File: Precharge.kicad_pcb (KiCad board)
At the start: 2 copper layers, 58 x 38 mm, 10 parts, among them J1 MicroFit+, J2 JST-XA, K1 DAR71205, Q1 BSS205N, U1 NCP1117

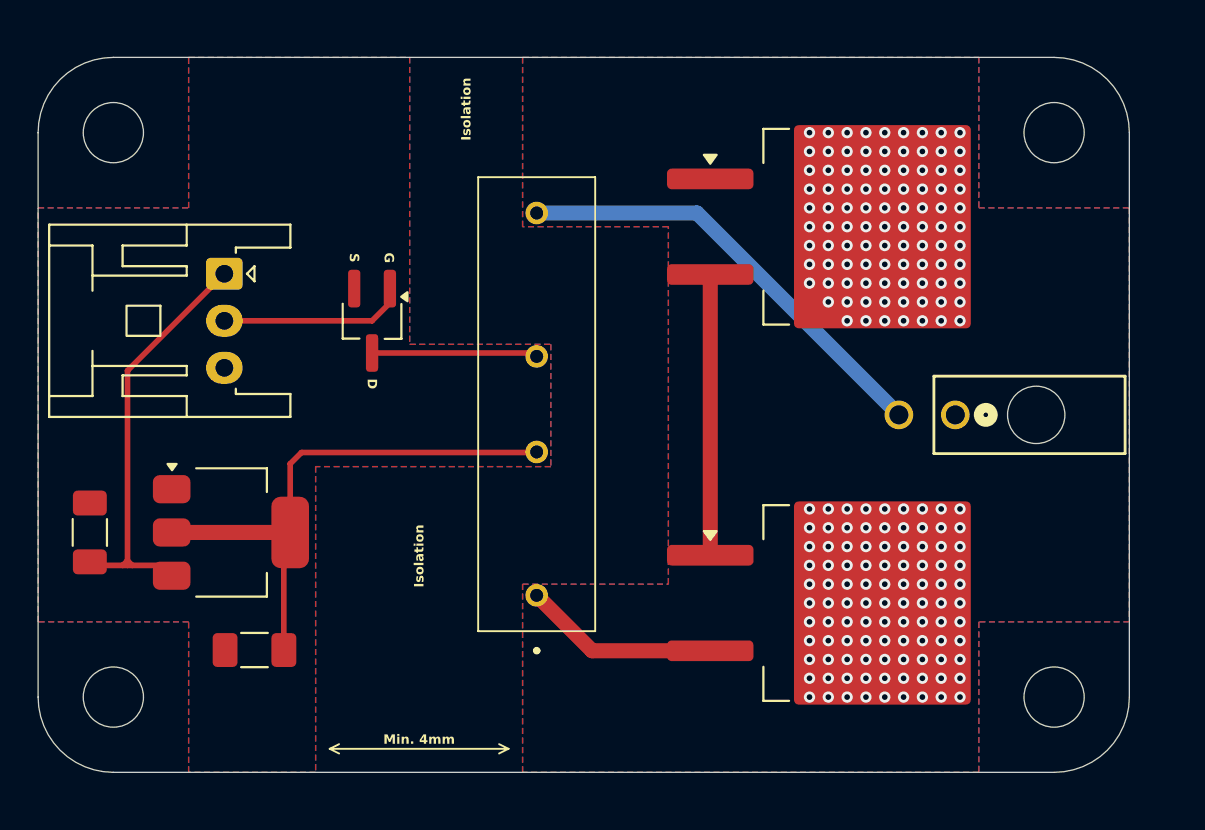
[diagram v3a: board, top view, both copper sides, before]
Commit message: TSAL compatibility, shortened precharge, simpler LV
Back to 4 resistors, so short precharge time, and powering relay from BMS GPIO. Cut SCS and regulation. added TSAL circuitry to allow for relay state measurement with single contact.
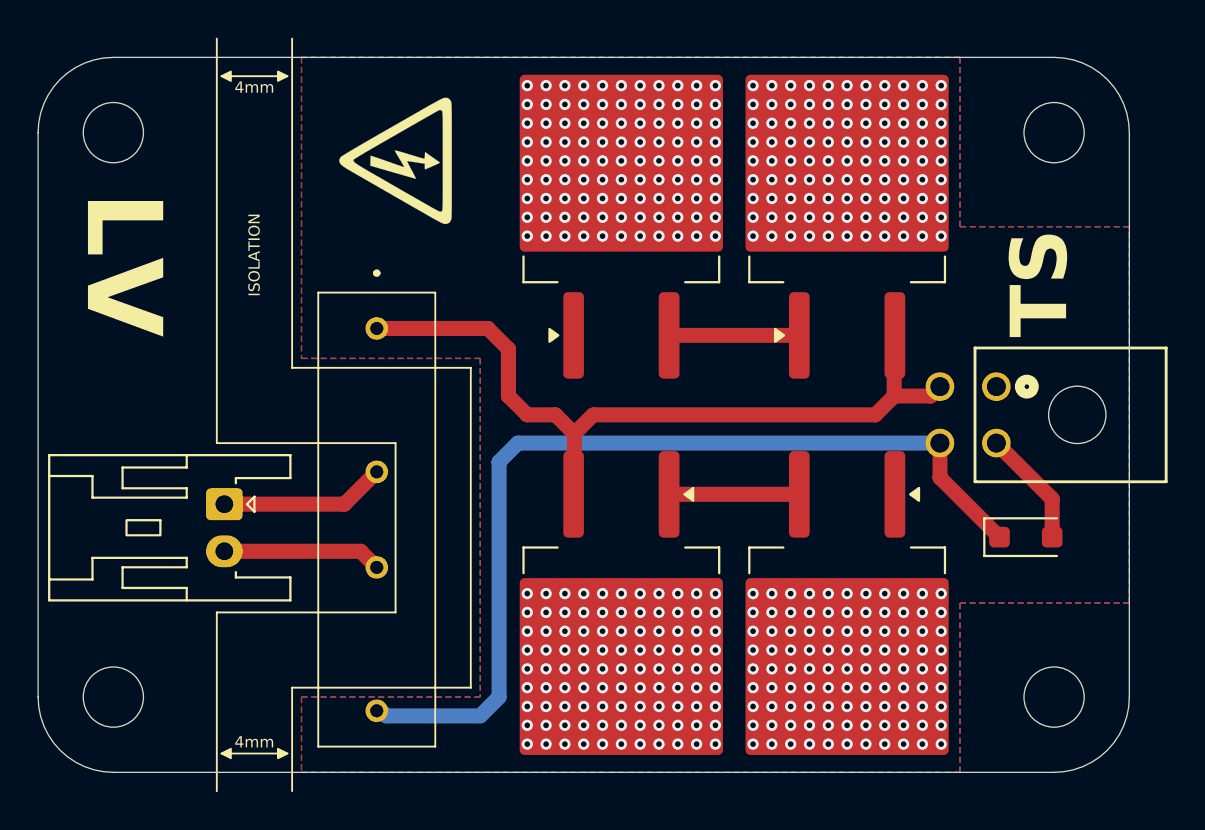
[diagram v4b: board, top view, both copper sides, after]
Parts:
- removed C1, C2: 10u, Library:C_1206_3216Metric_Pad1.33x1.80mm_HandSolder
- removed Q1: BSS205N, Library:MOSFET_Single_SOT-23
- removed U1: NCP1117, Library:Regulator_Linear_SOT-223-4
- added D1: 1.7V, Diode_SMD:D_SOD-123F, F.Cu at (197.5, 99.6)
- added G***: LOGO, Custom_MSM:Decorative_Hazard, F.Cu at (164.0, 79.6)
- added G***: LOGO, Custom_MSM:Decorative_Hazard, B.Cu at (164.0, 79.6)
- added R2: 5K, Package_TO_SOT_SMD:TO-263-2, F.Cu at (188.0, 105.0)
- added R4: 5K, Package_TO_SOT_SMD:TO-263-2, F.Cu at (176.0, 105.0)
- J1: footprint Library:Connector_MicroFit-Plus_2POS -> Custom_MSM:Connector_MicroFit-Plus_4POS
- J2: footprint Library:Connector_JST-XA_3POS -> Custom_MSM:Connector_JST-XA_2POS
- moved R3 21.9 mm to (188.0, 81.2), turned to 90 degrees
- moved R1 12.5 mm to (176.0, 81.2), turned to 90 degrees
- moved J2 12.2 mm to (154.9, 97.9)
- moved K1 9.86 mm to (163.0, 98.1), turned to -90 degrees
- moved J1 2.65 mm to (195.9, 91.6)
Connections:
- J2 pad 1: LVS -> /PC_5V
- J2 pad 2: /PC_En -> GND
- K1 pad 1: Net-(K1-Pad1) -> /Relay-
- K1 pad 2: +12VREG -> /PC_5V
- K1 pad 3: Net-(Q1-D) -> GND
- K1 pad 4: BATT+ -> /Relay+
- R3 pad 3: Net-(K1-Pad1) -> /Relay-
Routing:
- net /Relay+: track 0.00 -> 49.8 mm
- net /Relay-: track 0.00 -> 41.2 mm
- net +12VREG: track 29.7 -> 0.00 mm
- net LVS: track 23.0 -> 0.00 mm
- net BATT+: track 23.7 -> 6.23 mm
- net Net-(K1-Pad1): track 10.4 -> 0.00 mm
- net /PC_En: track 9.95 -> 0.00 mm
- net Net-(Q1-D): track 8.83 -> 0.00 mm
- net /PC_5V: track 0.00 -> 8.81 mm
- net GND: track 0.00 -> 8.46 mm
- net Net-(R1-Pad3): track 14.9 -> 6.92 mm
- net Net-(R2-Pad3): track 0.00 -> 6.92 mm
- net VEH+: track 0.00 -> 0.09 mm, vias 195 -> 396
- removed copper zone on B.Cu, net GND
- removed copper zone on F.Cu, net GND
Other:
- board text added: "4mm"
- board text added: "Credit card for scale"
- board text added: "ISOLATION"
- board text added: "LV"
- board text added: "TS"
- board text removed: "Isolation"
- board text removed: "Min. 4mm"
